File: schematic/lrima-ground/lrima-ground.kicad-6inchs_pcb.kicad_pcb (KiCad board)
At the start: 2 copper layers, 31.2 x 163.1 mm, 10 parts, among them J1 Finger Join

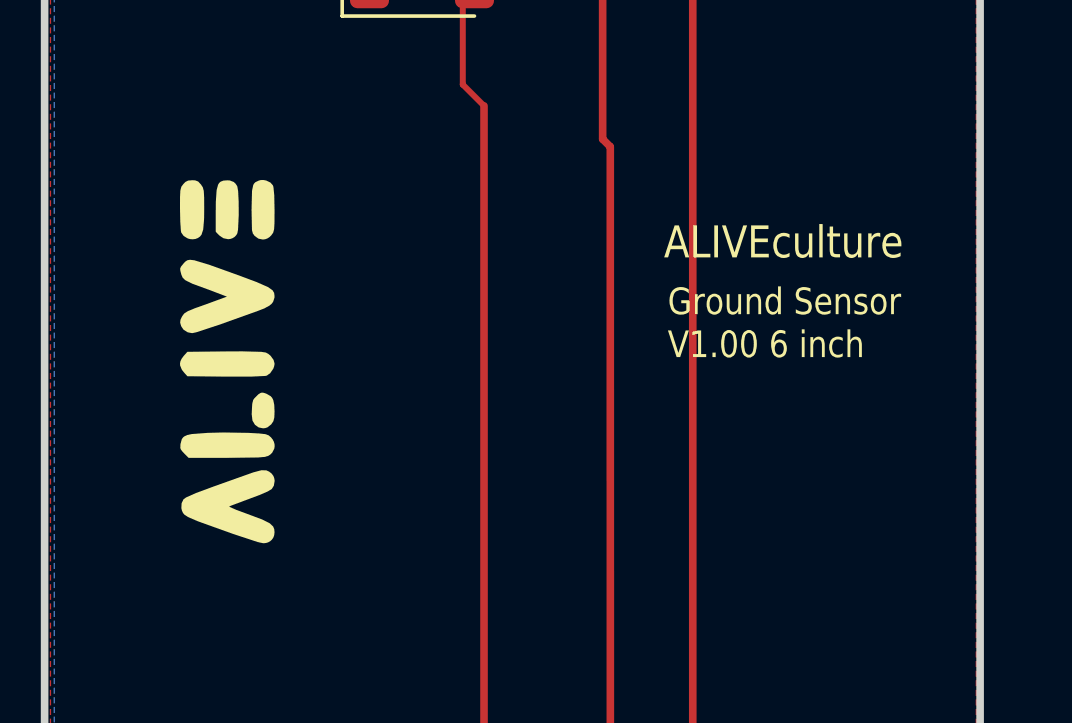
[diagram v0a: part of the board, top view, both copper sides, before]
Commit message: fix(pcb): Changed ALIVE to LRIMa
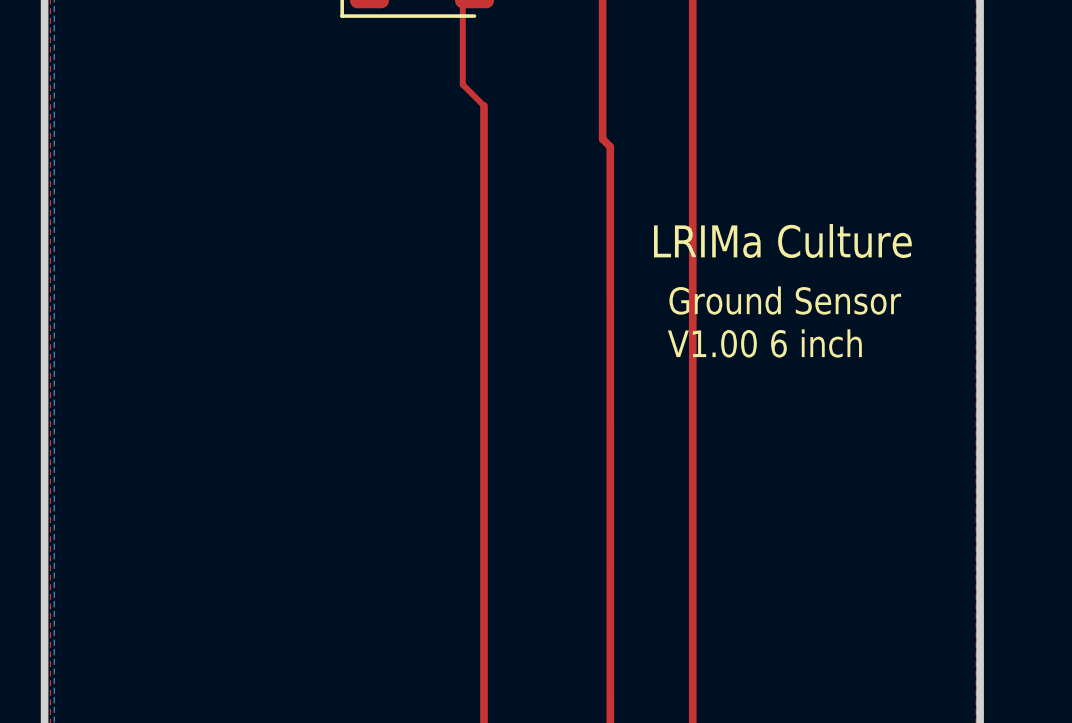
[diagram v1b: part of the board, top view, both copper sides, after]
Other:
- board text added: "LRIMa Culture"
- board text removed: "ALIVEculture"
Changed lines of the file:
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@@
 		(net 1)
-	)
-	(gr_poly
-		(pts
-			(xy 138.864277 46.322833) (xy 138.94307 46.437226) (xy 139.077853 46.521327) (xy 139.161919 46.545001)
-			(xy 139.249038 46.552005) (xy 139.332442 46.541658) (xy 139.411297 46.513245) (xy 139.420596 46.508394)
-			(xy 139.490153 46.459939) (xy 139.543047 46.39282) (xy 139.597969 46.224166) (xy 139.627078 45.877352)
-			(xy 139.631208 45.54095) (xy 139.629163 45.156584) (xy 139.616734 44.93946) (xy 139.584481 44.818965)
-			(xy 139.522965 44.724485) (xy 139.431435 44.62578) (xy 139.330842 44.587168) (xy 139.228444 44.581941)
-			(xy 139.093709 44.593702) (xy 139.000349 44.642288) (xy 138.932244 44.71352) (xy 138.868957 44.800897)
-			(xy 138.836271 44.917847) (xy 138.824512 45.138859) (xy 138.824 45.53842) (xy 138.833512 45.98077)
-			(xy 138.854189 46.274097)
-		)
-		(stroke
-			(width 0)
-			(type default)
-		)
-		(fill yes)
-		(layer "F.SilkS")
-	)
-	(gr_poly
-		(pts
-			(xy 141.238911 52.593926) (xy 141.322817 52.733802) (xy 141.448444 52.823618) (xy 141.59887 52.852955)
-			(xy 141.675019 52.842363) (xy 141.748657 52.814375) (xy 141.865713 52.719601) (xy 141.937479 52.613279)
-			(xy 141.968838 52.485529) (xy 141.975635 52.280161) (xy 141.965757 52.066352) (xy 141.933175 51.912298)
-			(xy 141.898478 51.840334) (xy 141.850986 51.783394) (xy 141.707125 51.699863) (xy 141.615835 51.668207)
-			(xy 141.552628 51.660432) (xy 141.497444 51.678276) (xy 141.430224 51.72348) (xy 141.299456 51.855945)
-			(xy 141.262405 51.912414) (xy 141.231345 52.039287) (xy 141.21334 52.370439)
-		)
-		(stroke
-			(width 0)
-			(type default)
-		)
-		(fill yes)
-		(layer "F.SilkS")
-	)
-	(gr_poly
-		(pts
-			(xy 138.961612 53.686202) (xy 139.11181 53.836337) (xy 140.375483 53.836337) (xy 141.422462 53.824213)
-			(xy 141.650093 53.804669) (xy 141.763344 53.772234) (xy 141.835676 53.725448) (xy 141.893669 53.668972)
-			(xy 141.966272 53.532055) (xy 141.978999 53.455754) (xy 141.975044 53.377817) (xy 141.954171 53.300726)
-			(xy 141.916067 53.226422) (xy 141.857323 53.153981) (xy 141.777714 53.085201) (xy 141.667897 53.045914)
-			(xy 141.460851 53.022917) (xy 141.089552 53.003003) (xy 140.262664 52.990422) (xy 139.754555 53.003003)
-			(xy 139.221053 53.042439) (xy 139.06258 53.076002) (xy 138.958012 53.126275) (xy 138.913359 53.169406)
-			(xy 138.881391 53.222961) (xy 138.839943 53.37581) (xy 138.833949 53.50982) (xy 138.855225 53.562415)
-			(xy 138.89848 53.619773)
-		)
-		(stroke
-			(width 0)
-			(type default)
-		)
-		(fill yes)
-		(layer "F.SilkS")
-	)
-	(gr_poly
-		(pts
-			(xy 138.966646 55.726521) (xy 139.090685 55.808284) (xy 139.424791 55.952568) (xy 140.612108 56.378513)
-			(xy 141.420052 56.644259) (xy 141.60056 56.683) (xy 141.685659 56.675456) (xy 141.762575 56.652376)
-			(xy 141.830047 56.615031) (xy 141.886414 56.564859) (xy 141.930077 56.50355) (xy 141.959885 56.43229)
-			(xy 141.975635 56.320314) (xy 141.965322 56.212477) (xy 141.926699 56.121966) (xy 141.812238 56.015101)
-			(xy 141.561497 55.8893) (xy 141.116403 55.723148) (xy 140.692694 55.566381) (xy 140.47454 55.46959)
-			(xy 140.466106 55.459989) (xy 140.517812 55.433414) (xy 141.134024 55.202735) (xy 141.481095 55.073241)
-			(xy 141.743763 54.959257) (xy 141.879978 54.878848) (xy 141.953253 54.762112) (xy 141.978575 54.60384)
-			(xy 141.967576 54.52039) (xy 141.939827 54.443256) (xy 141.879978 54.36181) (xy 141.792058 54.292535)
-			(xy 141.700699 54.253151) (xy 141.540011 54.248443) (xy 141.276369 54.317679) (xy 141.20283 54.343254)
-			(xy 141.039824 54.40138) (xy 139.929926 54.797033) (xy 139.345814 55.013742) (xy 139.025039 55.156968)
-			(xy 138.939795 55.218761) (xy 138.878219 55.350126) (xy 138.869536 55.516902) (xy 138.889374 55.600045)
-			(xy 138.925444 55.674942)
-		)
-		(stroke
-			(width 0)
-			(type default)
-		)
-		(fill yes)
-		(layer "F.SilkS")
-	)
-	(gr_poly
-		(pts
-			(xy 141.31359 46.43923) (xy 141.440535 46.530685) (xy 141.588282 46.559728) (xy 141.66437 46.549443)
-			(xy 141.737915 46.522371) (xy 141.805334 46.479536) (xy 141.865713 46.420674) (xy 141.928907 46.332968)
-			(xy 141.96158 46.21371) (xy 141.973799 45.98644) (xy 141.975635 45.574688) (xy 141.966108 45.082543)
-			(xy 141.938421 44.807923) (xy 141.921094 44.753162) (xy 141.840494 44.660726) (xy 141.694626 44.590561)
-			(xy 141.605482 44.574501) (xy 141.517032 44.576512) (xy 141.454558 44.591219) (xy 141.336704 44.648192)
-			(xy 141.295361 44.689385) (xy 141.263951 44.746188) (xy 141.224821 44.935232) (xy 141.208703 45.570471)
-			(xy 141.222444 46.24144) (xy 141.25366 46.360894)
-		)
-		(stroke
-			(width 0)
-			(type default)
-		)
-		(fill yes)
-		(layer "F.SilkS")
-	)
-	(gr_poly
-		(pts
-			(xy 138.864277 49.451211) (xy 138.942825 49.564349) (xy 139.081614 49.651846) (xy 139.230122 49.680631)
-			(xy 139.375298 49.64946) (xy 140.169066 49.387108) (xy 141.395821 48.947668) (xy 141.634553 48.855347)
-			(xy 141.802115 48.764579) (xy 141.876863 48.702948) (xy 141.928667 48.636129) (xy 141.972095 48.497716)
-			(xy 141.974796 48.438221) (xy 141.96185 48.337633) (xy 141.909309 48.250601) (xy 141.759481 48.144425)
-			(xy 141.382082 47.977653) (xy 140.758949 47.7449) (xy 140.753764 47.743014) (xy 139.804627 47.402366)
-			(xy 139.298625 47.24996) (xy 139.158381 47.233384) (xy 139.064814 47.250717) (xy 138.996558 47.297571)
-			(xy 138.932244 47.369562) (xy 138.919142 47.385234) (xy 138.85518 47.465942) (xy 138.829223 47.526784)
-			(xy 138.83514 47.600652) (xy 138.866794 47.72044) (xy 138.910773 47.827435) (xy 139.001761 47.915944)
-			(xy 139.233562 48.030757) (xy 139.814131 48.243382) (xy 140.38807 48.462681) (xy 139.757912 48.693788)
-			(xy 139.319957 48.850065) (xy 139.078665 48.949566) (xy 138.960721 49.028508) (xy 138.892806 49.123107)
-			(xy 138.838111 49.236832) (xy 138.829476 49.33462)
-		)
-		(stroke
-			(width 0)
-			(type default)
-		)
-		(fill yes)
-		(layer "F.SilkS")
 	)
 	(gr_line
@@
 			(type default)
 		)
-		(layer "F.SilkS")
-	)
-	(gr_poly
-		(pts
-			(xy 138.945669 50.976178) (xy 139.070694 51.116192) (xy 140.339402 51.128844) (xy 141.217239 51.128182)
-			(xy 141.666944 51.106027) (xy 141.719711 51.094262) (xy 141.830743 51.014911) (xy 141.934561 50.863003)
-			(xy 141.96473 50.778903) (xy 141.975635 50.696995) (xy 141.944744 50.57424) (xy 141.842368 50.432523)
-			(xy 141.768949 50.371696) (xy 141.686987 50.326718) (xy 141.534775 50.302366) (xy 140.89259 50.28615)
-			(xy 140.317586 50.288763) (xy 139.070694 50.301415) (xy 138.945669 50.441428) (xy 138.880322 50.528065)
-			(xy 138.83971 50.612953) (xy 138.824625 50.684473) (xy 138.827474 50.755821) (xy 138.884657 50.896425)
-		)
-		(stroke
-			(width 0)
-			(type default)
-		)
-		(fill yes)
-		(layer "F.SilkS")
-	)
-	(gr_poly
-		(pts
-			(xy 140.139699 46.427422) (xy 140.273077 46.517398) (xy 140.428434 46.54752) (xy 140.506976 46.538023)
-			(xy 140.580591 46.512078) (xy 140.644374 46.47159) (xy 140.697868 46.416374) (xy 140.735455 46.353198)
-			(xy 140.759355 46.224787) (xy 140.781865 45.739118) (xy 140.779812 45.307024) (xy 140.761743 44.946669)
-			(xy 140.732937 44.782683) (xy 140.679427 44.700355) (xy 140.617074 44.641602) (xy 140.485561 44.590733)
-			(xy 140.398978 44.584471) (xy 140.270028 44.59481) (xy 140.173143 44.633447) (xy 140.129249 44.67413)
-			(xy 140.094076 44.730979) (xy 140.044286 44.91533) (xy 140.018123 45.302766) (xy 140.015513 45.589027)
-			(xy 140.015513 46.301747)
-		)
-		(stroke
-			(width 0)
-			(type default)
-		)
-		(fill yes)
 		(layer "F.SilkS")
 	)
@@
 		)
 	)
-	(gr_text "ALIVEculture"
-		(at 154.953 47.285 360)
+	(gr_text "LRIMa Culture"
+		(at 154.5 47.285 0)
 		(layer "F.SilkS")
 		(effects
@@
 		)
 	)
-	(group ""
-		(members "13c14d3e-b4ac-4317-99dc-5f66cf0b5694" "261381e1-1326-4409-94c7-e8b6b5a5933e"
-			"3f2ddad0-185c-4bbc-b505-51a2bf6afa24" "8c26503b-e5d1-4fef-8706-e255984c3c75"
-			"cc2c25c0-59fe-40e6-91fb-7a2a456b9b99" "d9feb033-3543-4abc-9d7e-bdf2d1fdabb7"
-			"ec3513de-f295-4006-aff1-cccd05fcf32f" "fbe33f30-4549-44f1-9893-c913f0b47dd4"
-		)
-	)
